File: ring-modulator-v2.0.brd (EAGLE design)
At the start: 34.3 x 24.1 mm, 26 parts, among them IC1 TL072D, U1 MC1496DR2G

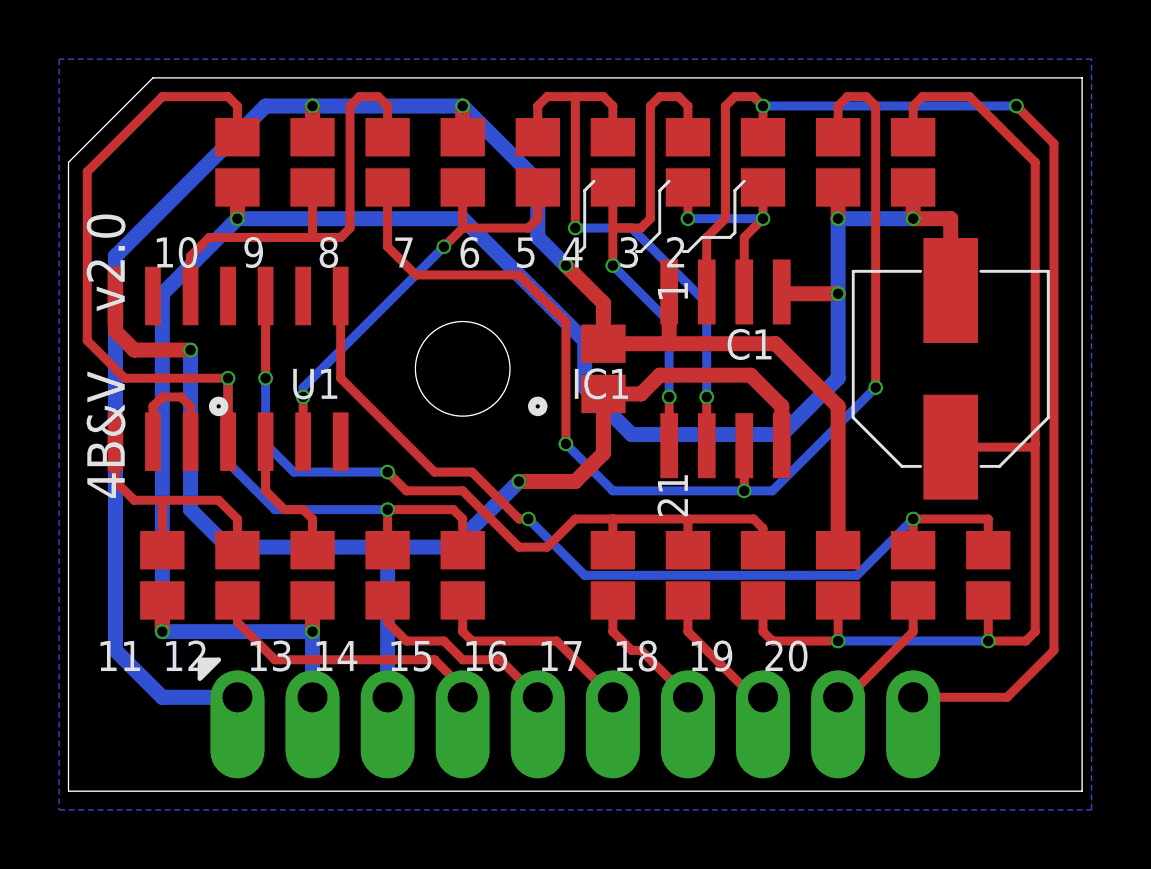
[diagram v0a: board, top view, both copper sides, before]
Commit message: Fixed silk screening, only missing xonik logo
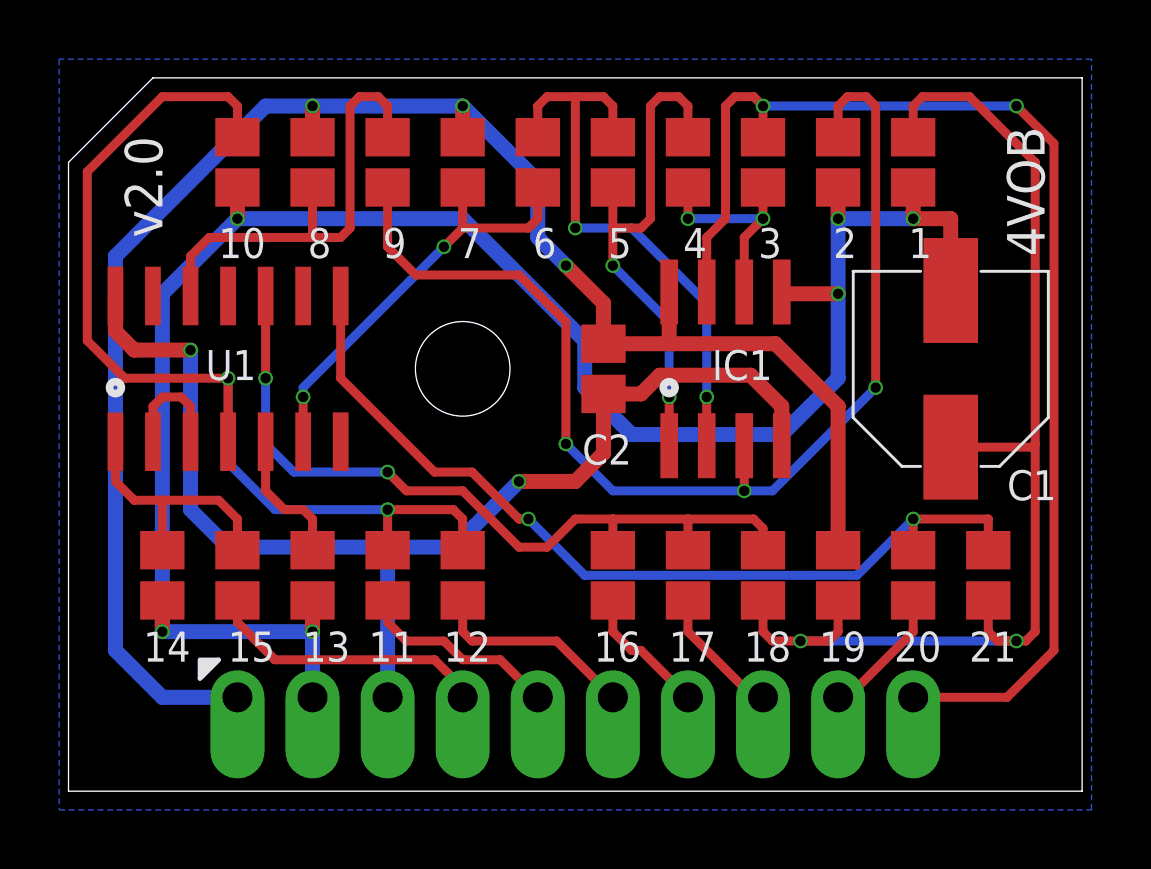
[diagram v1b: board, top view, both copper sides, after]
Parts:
- renumbered C5 to C2
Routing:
- net N$9: track 38.3 -> 40.1 mm
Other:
- board text added: "4VOB"
- board text added: "C2"
- board text added: "RING MODULATOR"
- board text removed: "4B&V"
- board text removed: "XRINGMOD"
